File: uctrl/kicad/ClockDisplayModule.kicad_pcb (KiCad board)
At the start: 2 copper layers, 94 x 58.4 mm, 48 parts, among them IC1 ATMEGA88PA-A, P101 CONN_02X03, P102 CONN_01X06, P201 CONN_01X06, P202 CONN_01X07, P203 CONN_01X06, P204 CONN_01X07, Q201 BC856BS, Q202 BC856BS, Q203 BC856BS, SW101 TL3315NF160Q, U201 SN74LS138, U202 74HC4511

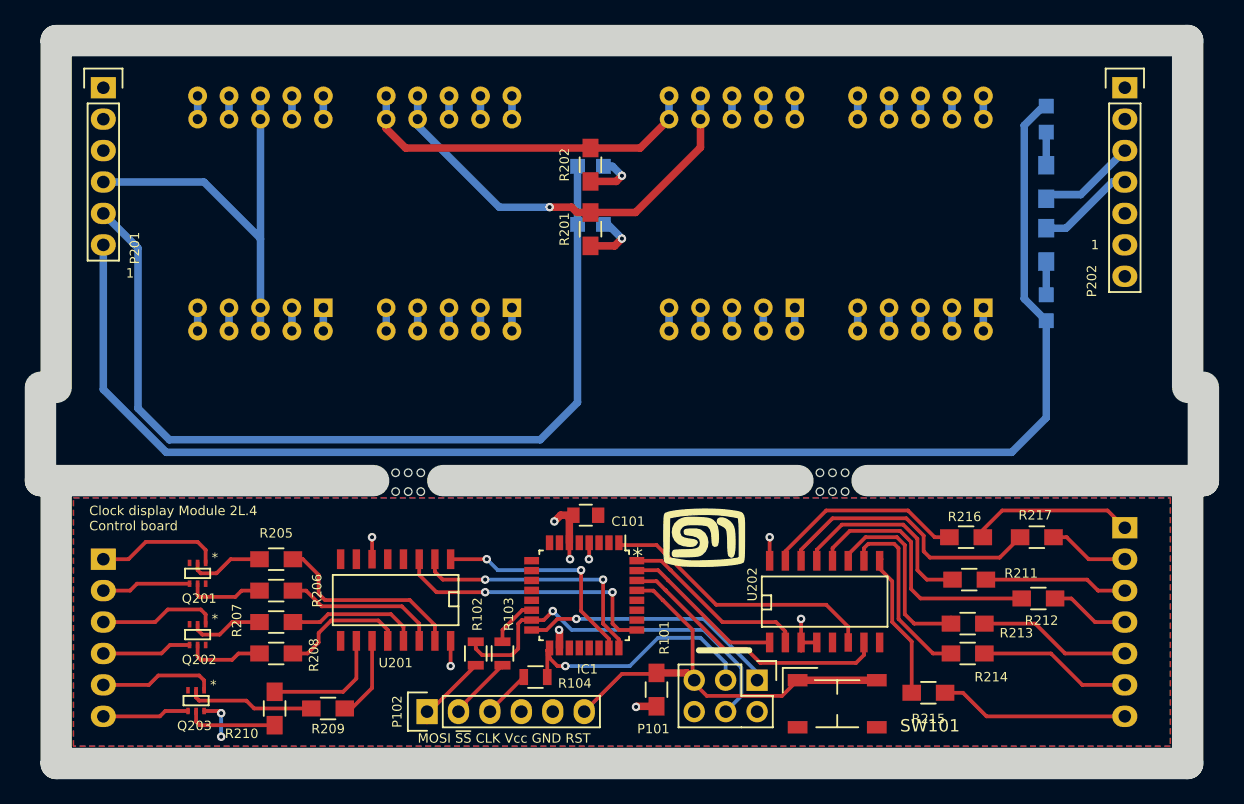
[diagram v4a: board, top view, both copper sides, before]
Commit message: Finished routing of revision 4
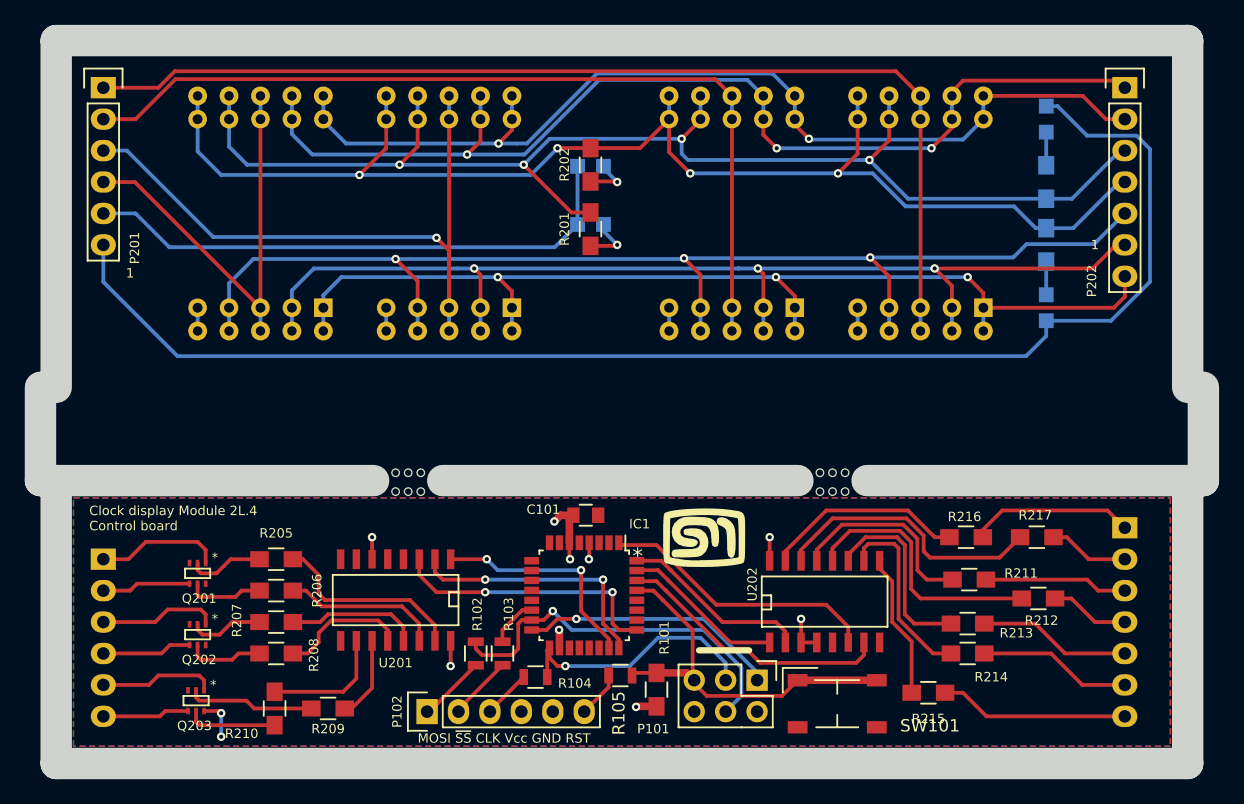
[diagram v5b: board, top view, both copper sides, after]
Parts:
- added R105: 0, Resistors_SMD:R_0805, F.Cu at (161.2, 93.2)
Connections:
- IC1 pad 10: Net-(IC1-Pad10) -> (no net)
- IC1 pad 11: Net-(IC1-Pad11) -> (no net)
- IC1 pad 12: Net-(IC1-Pad12) -> (no net)
- IC1 pad 13: Net-(IC1-Pad13) -> (no net)
- IC1 pad 19: Net-(IC1-Pad19) -> (no net)
- IC1 pad 2: Net-(IC1-Pad2) -> (no net)
- IC1 pad 20: Net-(IC1-Pad20) -> (no net)
- IC1 pad 22: Net-(IC1-Pad22) -> (no net)
- IC1 pad 26: Net-(IC1-Pad26) -> (no net)
- IC1 pad 27: Net-(IC1-Pad27) -> (no net)
- IC1 pad 28: Net-(IC1-Pad28) -> (no net)
- IC1 pad 7: Net-(IC1-Pad7) -> (no net)
- IC1 pad 8: Net-(IC1-Pad8) -> (no net)
- IC1 pad 9: Net-(IC1-Pad9) -> (no net)
- P102 pad 6: Reset -> Net-(P102-Pad6)
- U201 pad 7: Net-(U201-Pad7) -> (no net)
- U201 pad 9: Net-(U201-Pad9) -> (no net)
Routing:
- net /Display Driver/Seg_C: track 7.52 -> 98.8 mm, vias 0 -> 3
- net D_Dig_0: track 3.76 -> 86.4 mm
- net /Display Driver/Seg_D: track 7.52 -> 88.4 mm, vias 0 -> 3
- net /Display Driver/Seg_F: track 7.52 -> 87.5 mm, vias 0 -> 3
- net /Display Driver/Seg_E: track 7.52 -> 83.7 mm, vias 0 -> 3
- net /Display Driver/Seg_G: track 7.52 -> 82.0 mm, vias 0 -> 2
- net D_Dig_1: track 3.76 -> 71.9 mm
- net /Display Driver/Seg_B: track 40.7 -> 104.9 mm, vias 0 -> 4
- net /Display Driver/Seg_A: track 46.2 -> 105.4 mm, vias 1 -> 4
- net D_Dig_2: track 3.76 -> 54.9 mm, vias 0 -> 1
- net D_Colon: track 73.8 -> 44.9 mm
- net Reset: track 36.4 -> 31.5 mm
- net D_Signal: track 117.9 -> 113.8 mm
- net Net-(P102-Pad6): track 0.00 -> 3.74 mm
- net D_Dig_3: track 33.6 -> 35.9 mm
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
